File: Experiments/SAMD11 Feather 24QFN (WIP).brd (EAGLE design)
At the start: 50.8 x 22.9 mm, 37 parts, among them IC1 ATSAMD11D14A-MUT, J1 10118193-0001LF, Q1 DMG341, SW1 SPST_TACT-KMR2, U1 AP2112-3.3, U2 MCP73831T-2ACI/OT, X1 JSTPH, X2 2x5 0.05" SWD

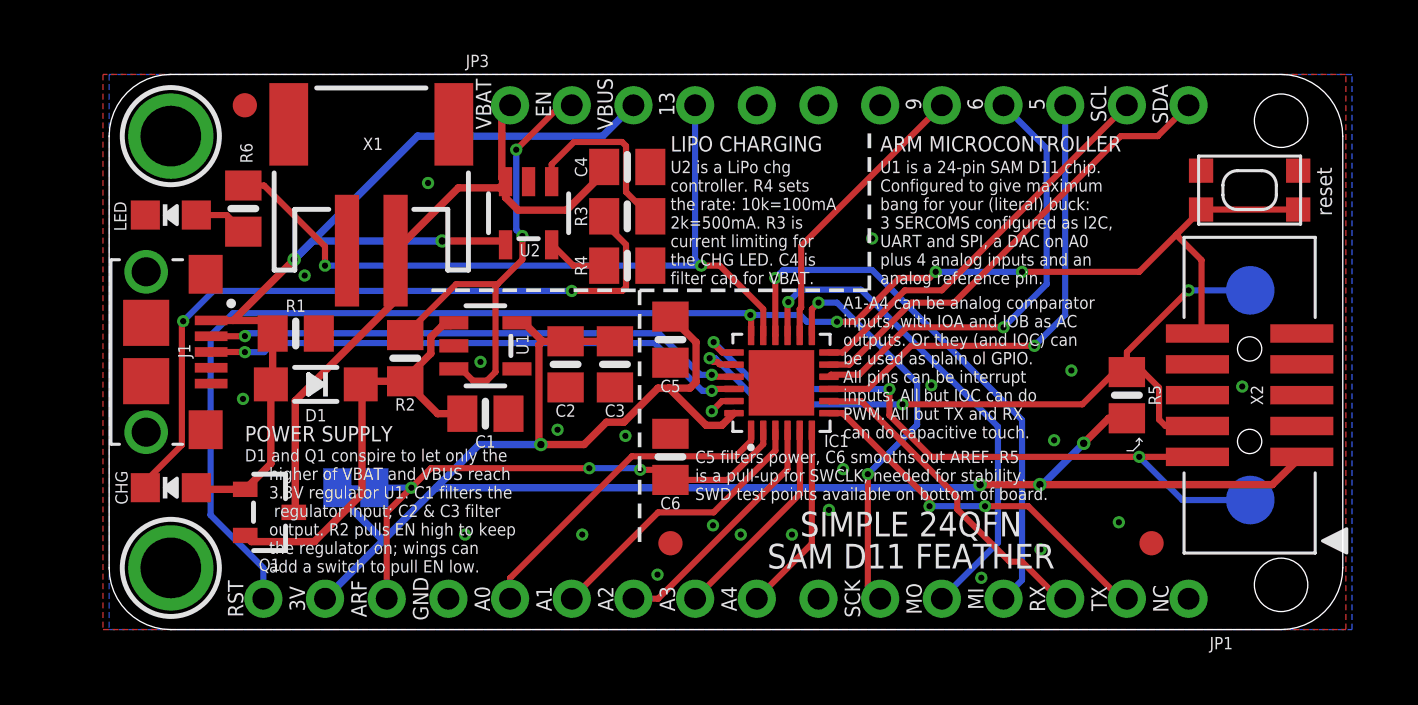
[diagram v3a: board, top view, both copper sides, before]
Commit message: swap miso and sck to match intended muxing
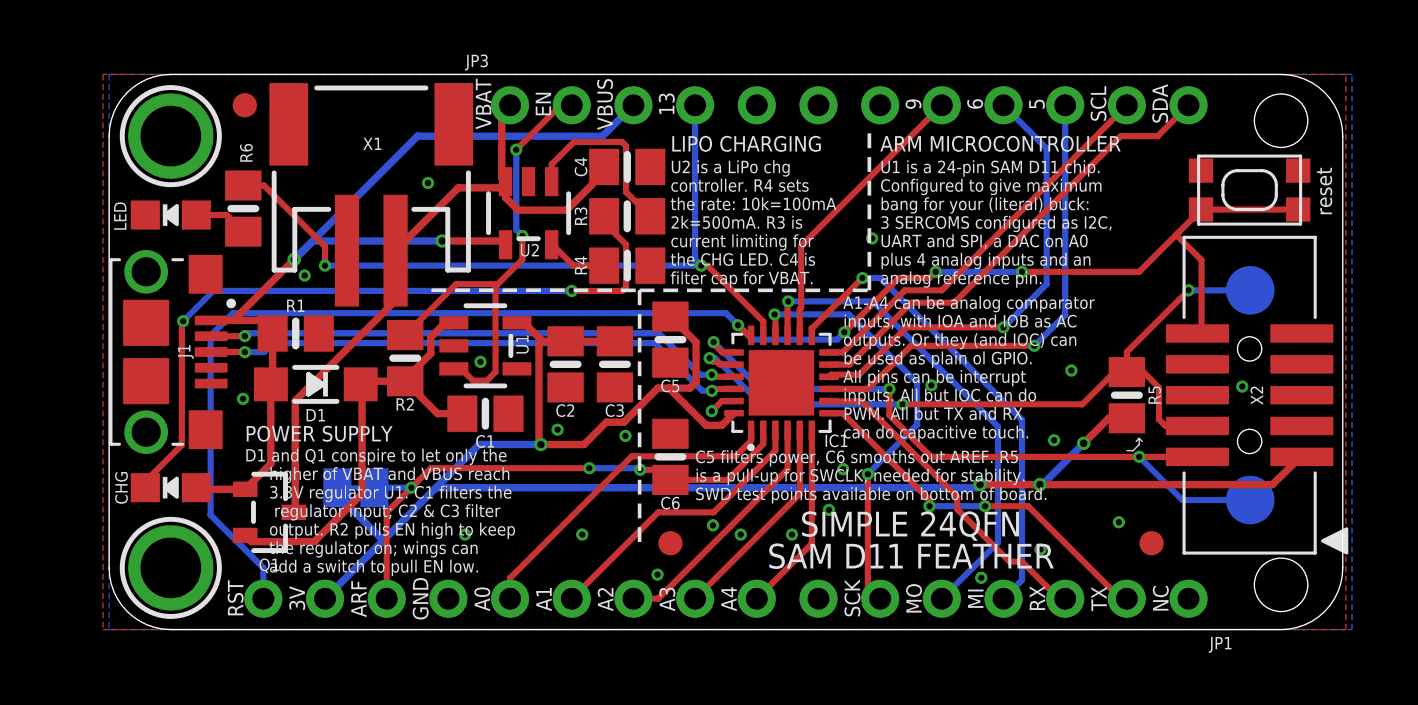
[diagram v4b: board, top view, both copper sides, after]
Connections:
- net MISO: now also IC1.13; no longer IC1.16
- net SCK: now also IC1.16; no longer IC1.13
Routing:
- net MISO: track 22.9 -> 19.9 mm
- net SCK: track 16.8 -> 17.9 mm
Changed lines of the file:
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@@
 <contactref element="JP1" pad="5"/>
 <contactref element="IC1" pad="15"/>
-<wire x1="27.936" y1="12.115" x2="27.936" y2="13.458" width="0.254" layer="1"/>
-<wire x1="27.936" y1="13.458" x2="27.9654" y2="13.4874" width="0.254" layer="1"/>
-<via x="27.9654" y="13.4874" extent="1-16" drill="0.254"/>
-<wire x1="27.9654" y1="13.4874" x2="28.4734" y2="13.9954" width="0.254" layer="16"/>
-<wire x1="28.4734" y1="13.9954" x2="30.9626" y2="13.9954" width="0.254" layer="16"/>
+<wire x1="27.936" y1="12.115" x2="27.936" y2="13.4834" width="0.254" layer="1"/>
+<wire x1="27.936" y1="13.4834" x2="27.9654" y2="13.5128" width="0.254" layer="1"/>
+<via x="27.9654" y="13.5128" extent="1-16" drill="0.254"/>
+<wire x1="27.9654" y1="13.5128" x2="31.4452" y2="13.5128" width="0.254" layer="16"/>
 <wire x1="36.6014" y1="8.3566" x2="36.6014" y2="3.5814" width="0.254" layer="16"/>
 <wire x1="36.6014" y1="3.5814" x2="34.29" y2="1.27" width="0.254" layer="16"/>
-<wire x1="30.9626" y1="13.9954" x2="36.6014" y2="8.3566" width="0.254" layer="16"/>
+<wire x1="31.4452" y1="13.5128" x2="36.6014" y2="8.3566" width="0.254" layer="16"/>
 </signal>
 <signal name="A5">
@@
 <signal name="MISO">
 <contactref element="JP1" pad="4"/>
-<contactref element="IC1" pad="16"/>
-<wire x1="27.436" y1="12.115" x2="27.432" y2="12.119" width="0.254" layer="1"/>
-<wire x1="27.432" y1="12.119" x2="27.432" y2="14.478" width="0.254" layer="1"/>
-<via x="27.432" y="14.478" extent="1-16" drill="0.254"/>
-<wire x1="27.432" y1="14.478" x2="27.7622" y2="14.8082" width="0.254" layer="16"/>
-<wire x1="27.7622" y1="14.8082" x2="31.4198" y2="14.8082" width="0.254" layer="16"/>
-<wire x1="31.4198" y1="14.8082" x2="37.592" y2="8.636" width="0.254" layer="16"/>
+<wire x1="31.75" y1="14.478" x2="37.592" y2="8.636" width="0.254" layer="16"/>
 <wire x1="37.592" y1="2.032" x2="36.83" y2="1.27" width="0.254" layer="16"/>
 <wire x1="37.592" y1="8.636" x2="37.592" y2="2.032" width="0.254" layer="16"/>
+<contactref element="IC1" pad="13"/>
+<wire x1="28.936" y1="12.115" x2="28.936" y2="12.39294375" width="0.254" layer="1"/>
+<wire x1="31.02105625" y1="14.478" x2="28.936" y2="12.39294375" width="0.254" layer="1"/>
+<via x="31.02105625" y="14.478" extent="1-16" drill="0.254"/>
+<wire x1="31.02105625" y1="14.478" x2="31.75" y2="14.478" width="0.254" layer="16"/>
 </signal>
 <signal name="SCK">
 <contactref element="JP1" pad="6"/>
-<contactref element="IC1" pad="13"/>
-<wire x1="28.936" y1="12.115" x2="28.936" y2="13.188" width="0.254" layer="1"/>
-<wire x1="28.936" y1="13.188" x2="29.21" y2="13.462" width="0.254" layer="1"/>
-<via x="29.21" y="13.462" extent="1-16" drill="0.254"/>
-<wire x1="29.21" y1="13.462" x2="29.972" y2="13.462" width="0.254" layer="16"/>
-<wire x1="29.972" y1="13.462" x2="33.274" y2="10.16" width="0.254" layer="16"/>
+<wire x1="30.45825625" y1="12.97574375" x2="33.274" y2="10.16" width="0.254" layer="16"/>
 <wire x1="33.274" y1="10.16" x2="33.274" y2="8.4328" width="0.254" layer="16"/>
 <wire x1="33.274" y1="8.4328" x2="31.242" y2="6.4008" width="0.254" layer="16"/>
@@
 <wire x1="31.242" y1="6.4008" x2="31.242" y2="1.778" width="0.254" layer="1"/>
 <wire x1="31.242" y1="1.778" x2="31.75" y2="1.27" width="0.254" layer="1"/>
+<contactref element="IC1" pad="16"/>
+<wire x1="27.436" y1="12.115" x2="27.436" y2="12.94234375" width="0.254" layer="1"/>
+<wire x1="27.436" y1="12.94234375" x2="27.4026" y2="12.97574375" width="0.254" layer="1"/>
+<via x="27.4026" y="12.97574375" extent="1-16" drill="0.254"/>
+<wire x1="27.4026" y1="12.97574375" x2="30.45825625" y2="12.97574375" width="0.254" layer="16"/>
 </signal>
 <signal name="A4">
@@
 <wire x1="8.8886" y1="14.986" x2="24.3826" y2="14.986" width="0.254" layer="16"/>
 <contactref element="IC1" pad="17"/>
-<wire x1="26.936" y1="12.115" x2="26.936" y2="13.196" width="0.254" layer="1"/>
-<wire x1="26.936" y1="13.196" x2="25.146" y2="14.986" width="0.254" layer="1"/>
-<wire x1="25.146" y1="14.986" x2="24.3826" y2="14.986" width="0.254" layer="1"/>
+<wire x1="26.936" y1="12.115" x2="26.936" y2="12.688" width="0.254" layer="1"/>
+<wire x1="26.936" y1="12.688" x2="24.638" y2="14.986" width="0.254" layer="1"/>
+<wire x1="24.638" y1="14.986" x2="24.3826" y2="14.986" width="0.254" layer="1"/>
 <via x="24.3826" y="14.986" extent="1-16" drill="0.254"/>
 <wire x1="24.13" y1="21.59" x2="24.13" y2="15.2386" width="0.254" layer="16"/>
@@
 <contactref element="JP1" pad="16"/>
 <contactref element="X2" pad="10"/>
-<wire x1="26.3264" y1="13.0302" x2="5.1054" y2="13.0302" width="0.254" layer="16"/>
+<wire x1="5.1054" y1="13.0302" x2="25.4" y2="13.0302" width="0.254" layer="16"/>
 <wire x1="5.1054" y1="13.0302" x2="4.175" y2="12.0998" width="0.254" layer="16"/>
 <wire x1="4.175" y1="12.0998" x2="4.175" y2="4.715" width="0.254" layer="16"/>
@@
 <wire x1="6.35" y1="2.54" x2="4.175" y2="4.715" width="0.254" layer="16"/>
 <contactref element="IC1" pad="18"/>
-<wire x1="26.436" y1="12.115" x2="26.436" y2="12.9206" width="0.254" layer="1"/>
-<wire x1="26.436" y1="12.9206" x2="26.4026" y2="12.954" width="0.254" layer="1"/>
-<via x="26.4026" y="12.954" extent="1-16" drill="0.254"/>
-<via x="29.972" y="12.6746" extent="1-16" drill="0.254"/>
-<wire x1="26.4026" y1="12.954" x2="28.45565625" y2="12.954" width="0.254" layer="16"/>
-<wire x1="28.45565625" y1="12.954" x2="28.73505625" y2="12.6746" width="0.254" layer="16"/>
-<wire x1="28.73505625" y1="12.6746" x2="29.972" y2="12.6746" width="0.254" layer="16"/>
-<wire x1="29.972" y1="12.6746" x2="30.734" y2="12.6746" width="0.254" layer="1"/>
-<wire x1="32.5374" y1="14.478" x2="30.734" y2="12.6746" width="0.254" layer="1"/>
-<wire x1="33.782" y1="14.478" x2="32.5374" y2="14.478" width="0.254" layer="1"/>
+<via x="30.2768" y="12.2428" extent="1-16" drill="0.254"/>
+<wire x1="32.512" y1="14.478" x2="30.2768" y2="12.2428" width="0.254" layer="1"/>
+<wire x1="33.782" y1="14.478" x2="32.512" y2="14.478" width="0.254" layer="1"/>
 <wire x1="33.782" y1="14.478" x2="34.036" y2="14.732" width="0.254" layer="1"/>
 <via x="34.036" y="14.732" extent="1-16" drill="0.254"/>
@@
 <wire x1="44.9834" y1="15.2146" x2="43.942" y2="16.256" width="0.254" layer="1"/>
 <wire x1="44.9646" y1="17.2975" x2="48.9646" y2="17.2975" width="0.254" layer="1"/>
-<wire x1="26.3264" y1="13.0302" x2="26.4026" y2="12.954" width="0.254" layer="16"/>
 <wire x1="43.942" y1="16.256" x2="42.418" y2="14.732" width="0.254" layer="1"/>
 <wire x1="42.418" y1="14.732" x2="37.592" y2="14.732" width="0.254" layer="1"/>
+<wire x1="25.4" y1="13.0302" x2="25.8953" y2="12.5349" width="0.254" layer="16"/>
+<wire x1="25.8953" y1="12.5349" x2="26.4922" y2="11.938" width="0.254" layer="16"/>
+<wire x1="29.972" y1="11.938" x2="30.2768" y2="12.2428" width="0.254" layer="16"/>
+<wire x1="26.4922" y1="11.938" x2="29.972" y2="11.938" width="0.254" layer="16"/>
+<wire x1="26.436" y1="12.115" x2="26.3152" y2="12.115" width="0.254" layer="1"/>
+<wire x1="26.3152" y1="12.115" x2="25.8953" y2="12.5349" width="0.254" layer="1"/>
+<via x="25.8953" y="12.5349" extent="1-16" drill="0.254"/>
 </signal>
 <signal name="SWDIO">
